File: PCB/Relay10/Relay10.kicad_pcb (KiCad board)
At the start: 2 copper layers, 46.5 x 37.5 mm, 43 parts, among them J1 USB-C, J10 O8, J11 O9, J12 O10, J2 POWER, J3 O1, J4 O2, J5 O3, J6 O4, J7 O5, J8 O6, J9 O7, U1 ESP32-PICO-MINI-02, U10 QR, U2 FT231XQ, U3 ISL89410, U4 ISL89410, U5 ISL89410, U6 ISL89410, U7 ISL89410, U8 LMR16006+FB, U9 AA

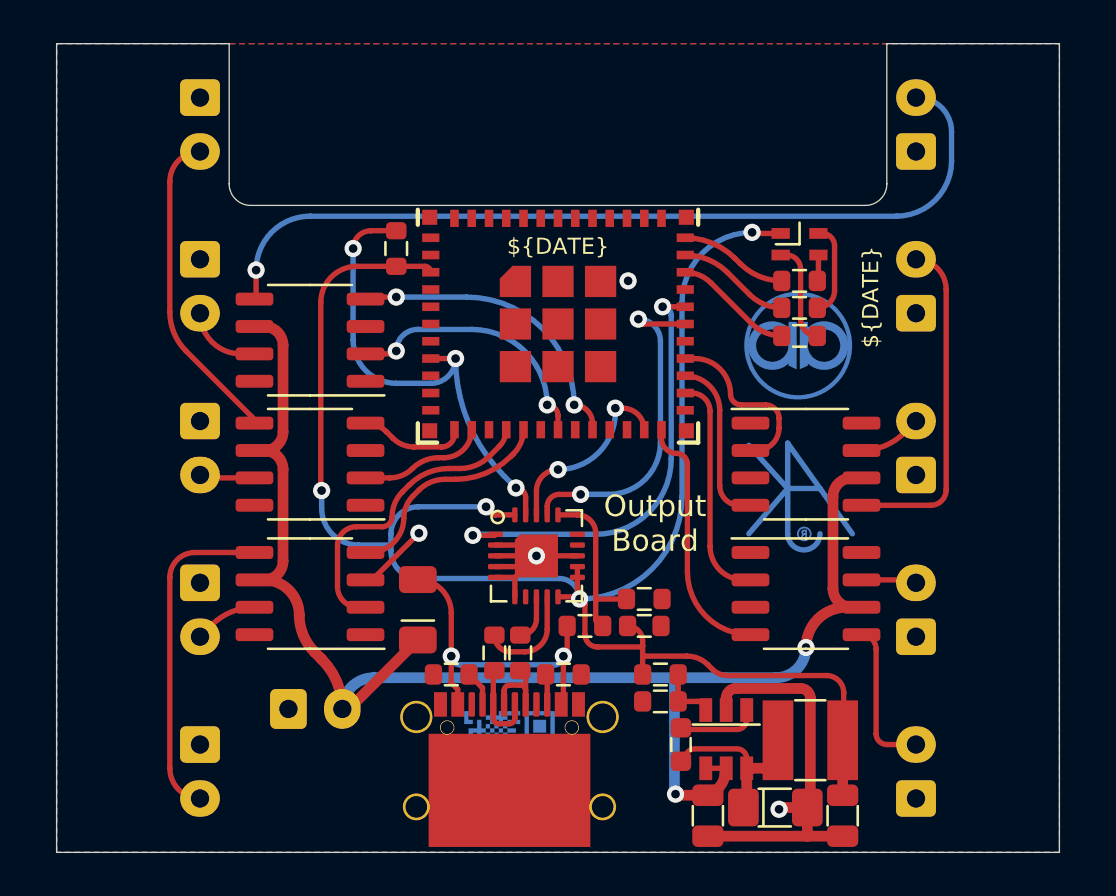
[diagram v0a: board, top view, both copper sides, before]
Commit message: Update Relay10 and document
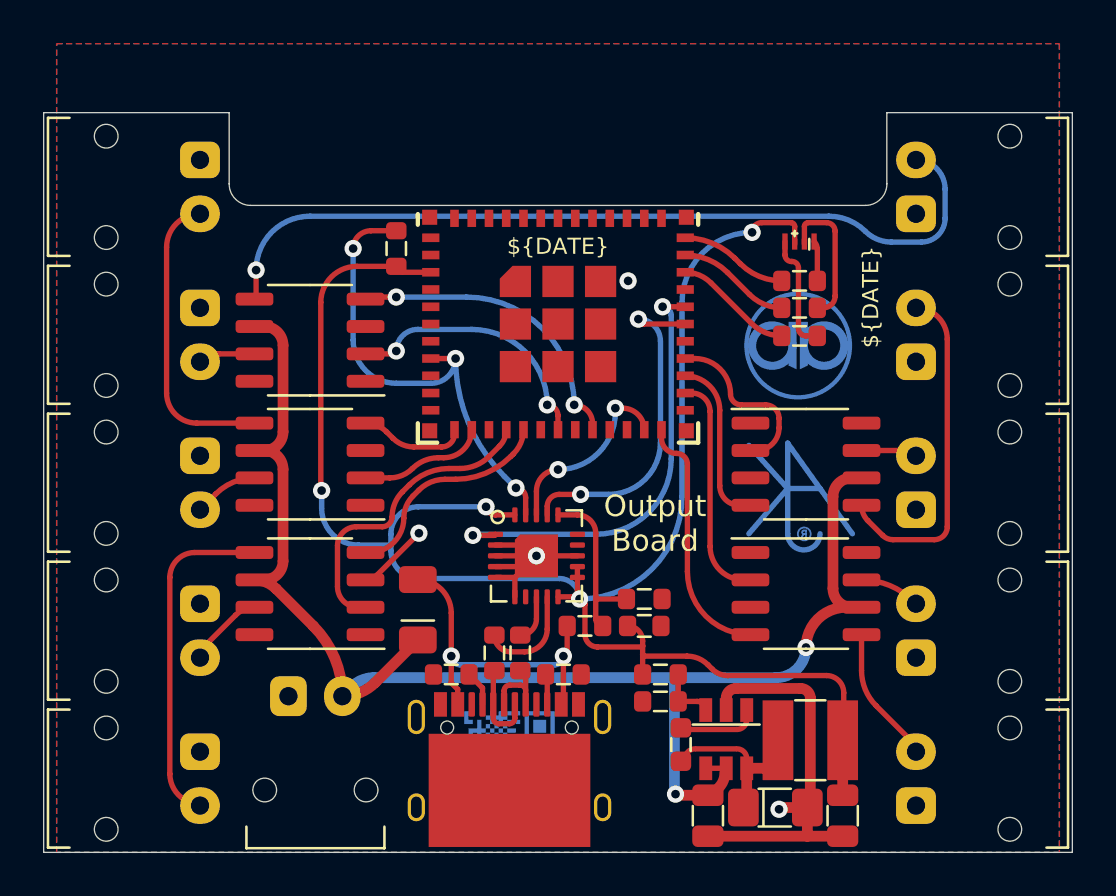
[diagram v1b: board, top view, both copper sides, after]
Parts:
- D1: value LED_RGBA -> LED_BARG; footprint RevK:LED-RGB-1.6x1.6 -> RevK:MHS190RGBCT
- J1: footprint RevK:USC16-TR-Round -> RevK:USC16-TR
- J10, J11, J12, J2, J3, J4, J5, J6, J7, J8, J9: footprint RevK:Molex_MiniSPOX_H2RA -> RevK:PTSM-HH1-2-RA
- R10: value 220R -> 100R
- R8: value 680R -> 300R
- R9: value 2K -> 1K
- moved J1 4.40 mm to (102.5, 56.1)
- moved J11 2.89 mm to (121.3, 29.6)
- moved J3 2.89 mm to (88.2, 29.6)
- moved J10 2.25 mm to (121.3, 36.5)
- moved J12 2.25 mm to (88.2, 36.5)
- moved J4 1.61 mm to (88.2, 43.4)
- moved J9 1.61 mm to (121.3, 43.4)
- moved J6 0.97 mm to (88.2, 50.2)
- moved J8 0.97 mm to (121.3, 50.2)
- moved J2 0.59 mm to (93.5, 53.3)
- moved J5 0.33 mm to (88.2, 57.1)
- moved J7 0.33 mm to (121.3, 57.1)
- turned D1 to 0 degrees
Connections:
- D1 pad 1: +3V3 -> Net-(D1-Pad1)
- D1 pad 2: Net-(D1-Pad2) -> +3V3
- R10 pad 1: Net-(D1-Pad4) -> Net-(D1-Pad1)
- R8 pad 1: Net-(D1-Pad2) -> Net-(D1-Pad3)
- R9 pad 1: Net-(D1-Pad3) -> Net-(D1-Pad4)
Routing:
- net Net-(D1-Pad1): track 0.00 -> 5.43 mm
- net Net-(D1-Pad3): track 1.23 -> 6.40 mm
- net Net-(D1-Pad2): track 4.35 -> 0.00 mm
- net +12V: track 69.9 -> 66.6 mm
- net Net-(D1-Pad4): track 4.78 -> 1.86 mm
- net O9: track 40.2 -> 38.9 mm
- net +3V3: track 81.9 -> 83.1 mm
- net O5: track 7.07 -> 5.80 mm
- net O7: track 2.96 -> 1.93 mm
- net O10: track 3.53 -> 2.62 mm
- net O1: track 14.8 -> 13.9 mm
- net GND: track 15.2 -> 14.5 mm
- net OUT8: track 7.85 -> 7.33 mm
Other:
- board size 46.5 x 37.5 mm -> 47.7 x 34.3 mm
